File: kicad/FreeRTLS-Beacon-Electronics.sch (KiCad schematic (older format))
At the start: 29 parts, among them J1 USB_B_Micro, J2 TC2030, U1 STM32F072CBTx, U2 NCP1117-3.3_SOT223, U3 DWM1001

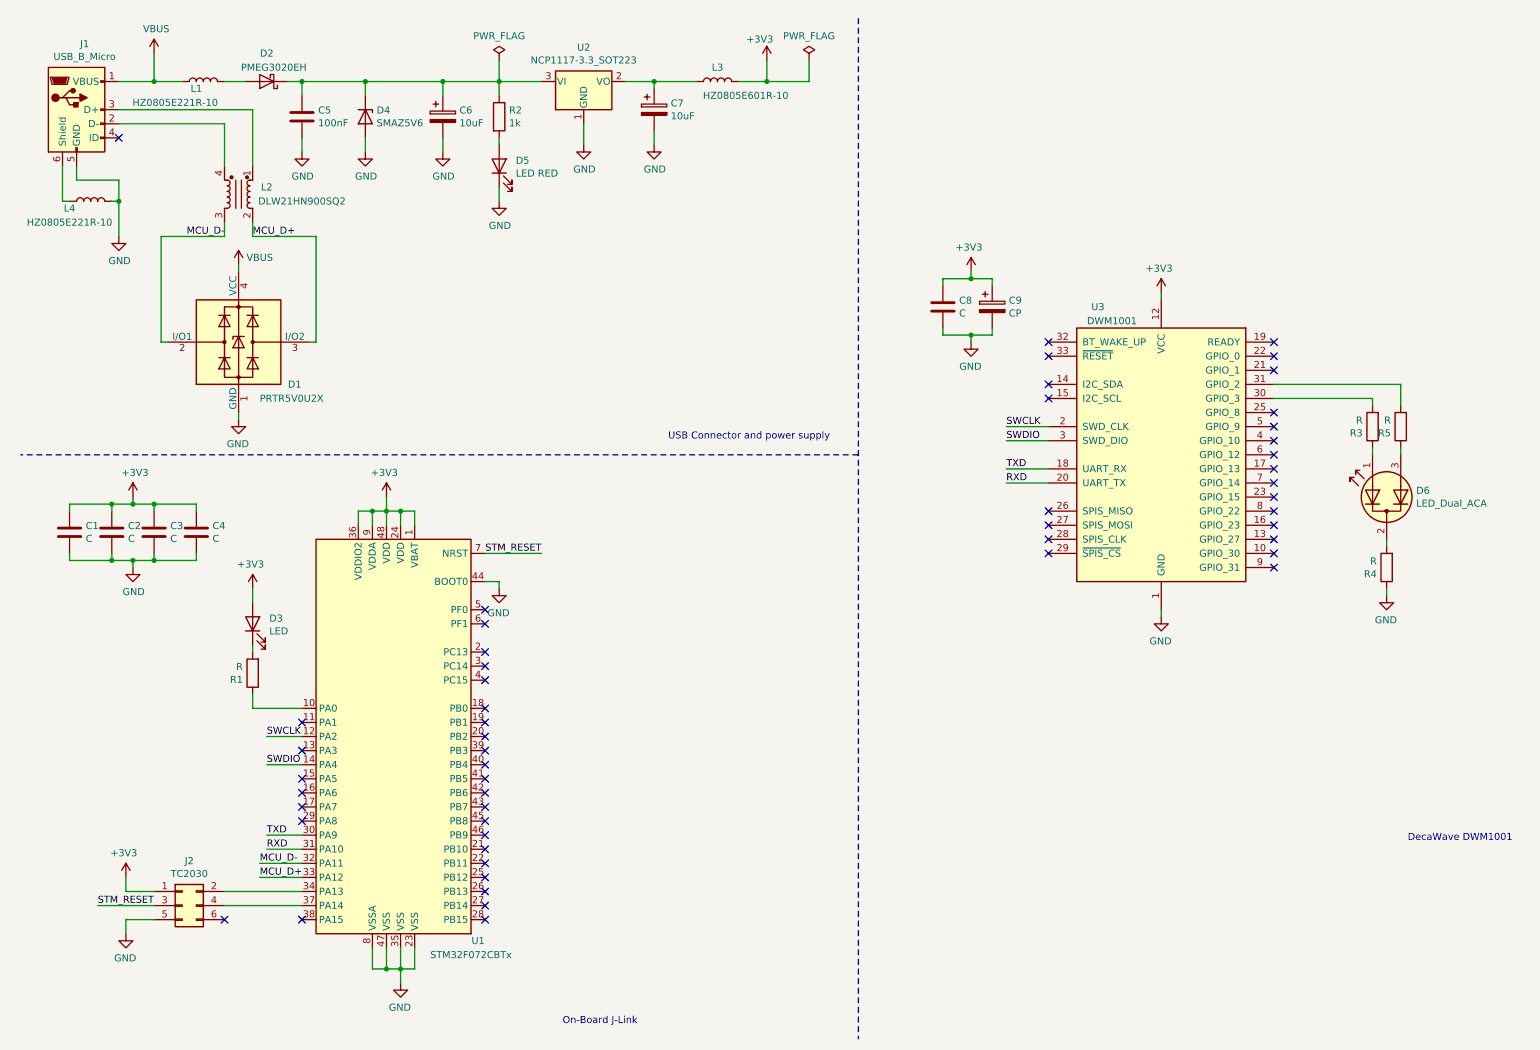
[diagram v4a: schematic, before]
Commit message: Add values and order labels
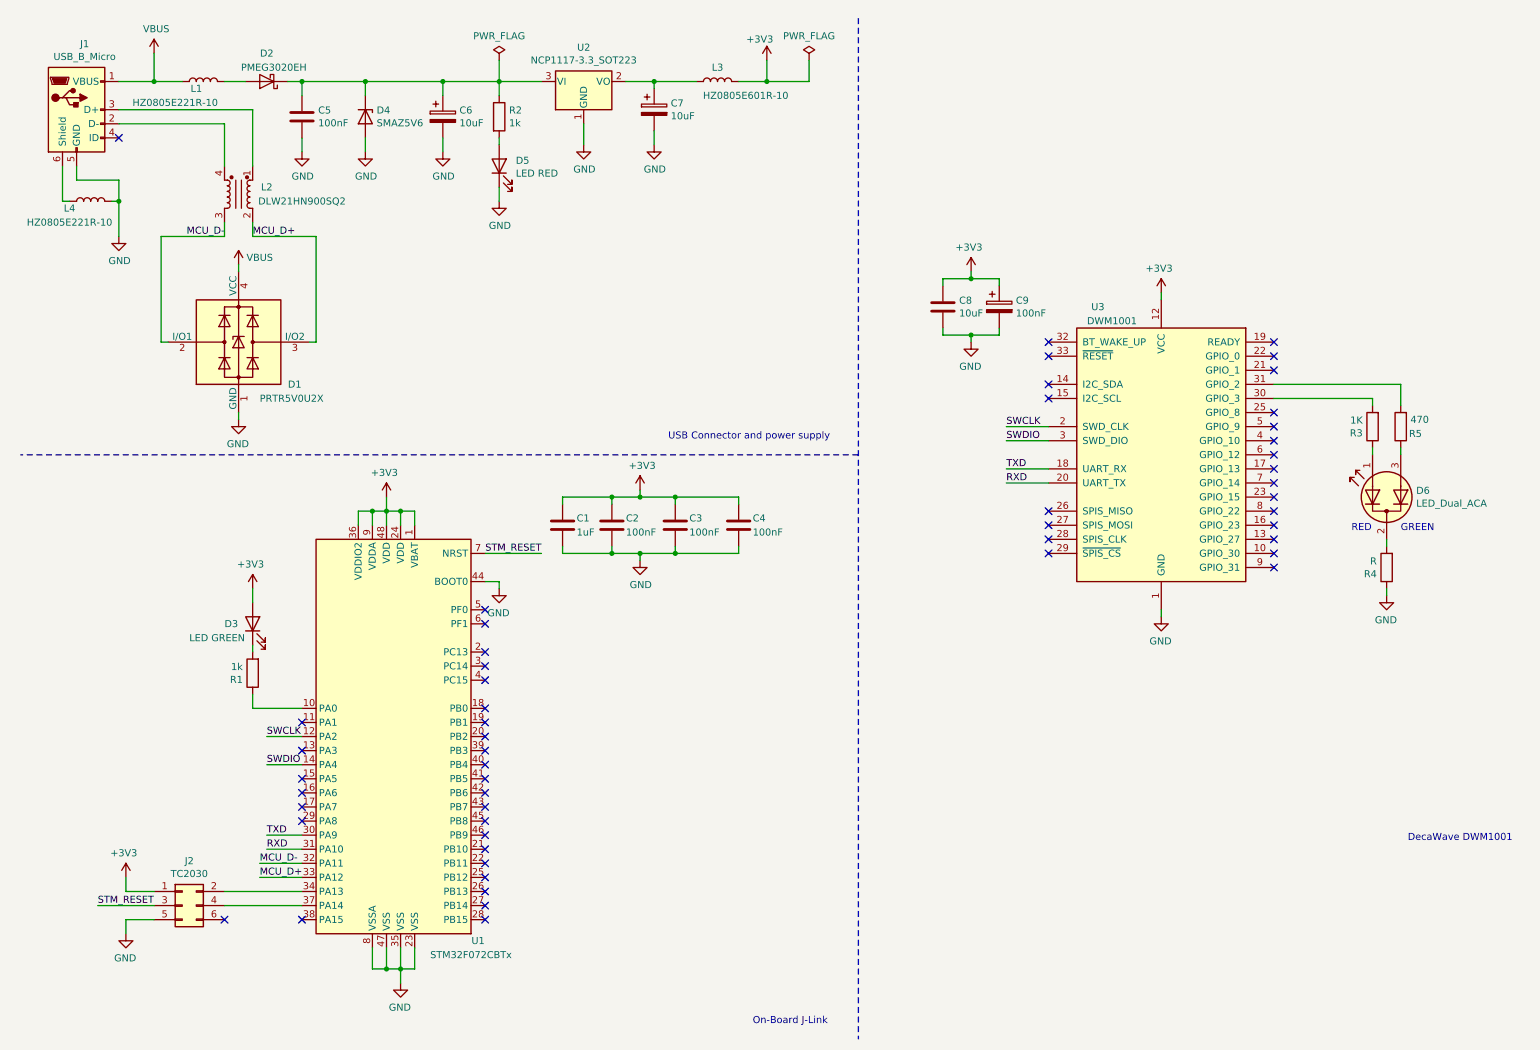
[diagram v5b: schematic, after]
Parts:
- C1: value C -> 1uF
- C2, C3, C4: value C -> 100nF
- C8: value C -> 10uF
- C9: value CP -> 100nF
- D3: value LED -> LED GREEN
- R1: value R -> 1k
- R3: value R -> 1K
- R5: value R -> 470
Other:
- note added: "GREEN"
- note added: "RED"
- moved on the sheet: C1, C2, C3, C4, C9
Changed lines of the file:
@@
 L Device:C C1
 U 1 1 5F5197C4
-P 850 4200
-F 0 "C1" H 965 4246 50  0000 L CNN
-F 1 "C" H 965 4155 50  0000 L CNN
-F 2 "" H 888 4050 50  0001 C CNN
-F 3 "~" H 850 4200 50  0001 C CNN
-	1    850  4200
+P 4350 4150
+F 0 "C1" H 4450 4200 50  0000 L CNN
+F 1 "1uF" H 4450 4100 50  0000 L CNN
+F 2 "" H 4388 4000 50  0001 C CNN
+F 3 "~" H 4350 4150 50  0001 C CNN
+	1    4350 4150
 	1    0    0    -1
 $EndComp
@@
 L Device:C C2
 U 1 1 5F51A6EE
-P 1150 4200
-F 0 "C2" H 1265 4246 50  0000 L CNN
-F 1 "C" H 1265 4155 50  0000 L CNN
-F 2 "" H 1188 4050 50  0001 C CNN
-F 3 "~" H 1150 4200 50  0001 C CNN
-	1    1150 4200
+P 4700 4150
+F 0 "C2" H 4800 4200 50  0000 L CNN
+F 1 "100nF" H 4800 4100 50  0000 L CNN
+F 2 "" H 4738 4000 50  0001 C CNN
+F 3 "~" H 4700 4150 50  0001 C CNN
+	1    4700 4150
 	1    0    0    -1
 $EndComp
@@
 L Device:C C3
 U 1 1 5F51B88B
-P 1450 4200
-F 0 "C3" H 1565 4246 50  0000 L CNN
-F 1 "C" H 1565 4155 50  0000 L CNN
-F 2 "" H 1488 4050 50  0001 C CNN
-F 3 "~" H 1450 4200 50  0001 C CNN
-	1    1450 4200
+P 5150 4150
+F 0 "C3" H 5250 4200 50  0000 L CNN
+F 1 "100nF" H 5250 4100 50  0000 L CNN
+F 2 "" H 5188 4000 50  0001 C CNN
+F 3 "~" H 5150 4150 50  0001 C CNN
+	1    5150 4150
 	1    0    0    -1
 $EndComp
@@
 L Device:C C4
 U 1 1 5F51B891
-P 1750 4200
-F 0 "C4" H 1865 4246 50  0000 L CNN
-F 1 "C" H 1865 4155 50  0000 L CNN
-F 2 "" H 1788 4050 50  0001 C CNN
-F 3 "~" H 1750 4200 50  0001 C CNN
-	1    1750 4200
-	1    0    0    -1
-$EndComp
-Wire Wire Line
-	850  4000 850  4050
-Wire Wire Line
-	850  4000 1150 4000
-Wire Wire Line
-	1750 4000 1750 4050
-Wire Wire Line
-	1450 4050 1450 4000
-Connection ~ 1450 4000
-Wire Wire Line
-	1450 4000 1750 4000
-Wire Wire Line
-	1150 4050 1150 4000
-Connection ~ 1150 4000
-Wire Wire Line
-	1150 4000 1300 4000
-Wire Wire Line
-	850  4350 850  4400
-Wire Wire Line
-	850  4400 1150 4400
-Wire Wire Line
-	1750 4400 1750 4350
-Wire Wire Line
-	1150 4350 1150 4400
-Wire Wire Line
-	1150 4400 1300 4400
-Wire Wire Line
-	1450 4350 1450 4400
-Connection ~ 1450 4400
-Wire Wire Line
-	1450 4400 1750 4400
+P 5600 4150
+F 0 "C4" H 5700 4200 50  0000 L CNN
+F 1 "100nF" H 5700 4100 50  0000 L CNN
+F 2 "" H 5638 4000 50  0001 C CNN
+F 3 "~" H 5600 4150 50  0001 C CNN
+	1    5600 4150
+	1    0    0    -1
+$EndComp
+Wire Wire Line
+	4350 3950 4350 4000
+Wire Wire Line
+	4350 3950 4700 3950
+Wire Wire Line
+	5600 3950 5600 4000
+Wire Wire Line
+	5150 4000 5150 3950
+Connection ~ 5150 3950
+Wire Wire Line
+	5150 3950 5600 3950
+Wire Wire Line
+	4700 4000 4700 3950
+Connection ~ 4700 3950
+Wire Wire Line
+	4700 3950 4900 3950
+Wire Wire Line
+	4350 4300 4350 4350
+Wire Wire Line
+	4350 4350 4700 4350
+Wire Wire Line
+	5600 4350 5600 4300
+Wire Wire Line
+	4700 4300 4700 4350
+Wire Wire Line
+	4700 4350 4900 4350
+Wire Wire Line
+	5150 4300 5150 4350
+Connection ~ 5150 4350
+Wire Wire Line
+	5150 4350 5600 4350
 $Comp
 L power:+3V3 #PWR05
 U 1 1 5F520C3E
-P 1300 3950
-F 0 "#PWR05" H 1300 3800 50  0001 C CNN
-F 1 "+3V3" H 1315 4123 50  0000 C CNN
-F 2 "" H 1300 3950 50  0001 C CNN
-F 3 "" H 1300 3950 50  0001 C CNN
-	1    1300 3950
-	1    0    0    -1
-$EndComp
-Wire Wire Line
-	1300 3950 1300 4000
-Connection ~ 1300 4000
-Wire Wire Line
-	1300 4000 1450 4000
+P 4900 3900
+F 0 "#PWR05" H 4900 3750 50  0001 C CNN
+F 1 "+3V3" H 4915 4073 50  0000 C CNN
+F 2 "" H 4900 3900 50  0001 C CNN
+F 3 "" H 4900 3900 50  0001 C CNN
+	1    4900 3900
+	1    0    0    -1
+$EndComp
+Wire Wire Line
+	4900 3900 4900 3950
+Connection ~ 4900 3950
+Wire Wire Line
+	4900 3950 5150 3950
 $Comp
 L power:GND #PWR06
 U 1 1 5F522893
-P 1300 4450
-F 0 "#PWR06" H 1300 4200 50  0001 C CNN
-F 1 "GND" H 1305 4277 50  0000 C CNN
-F 2 "" H 1300 4450 50  0001 C CNN
-F 3 "" H 1300 4450 50  0001 C CNN
-	1    1300 4450
-	1    0    0    -1
-$EndComp
-Wire Wire Line
-	1300 4450 1300 4400
-Connection ~ 1300 4400
-Wire Wire Line
-	1300 4400 1450 4400
+P 4900 4400
+F 0 "#PWR06" H 4900 4150 50  0001 C CNN
+F 1 "GND" H 4905 4227 50  0000 C CNN
+F 2 "" H 4900 4400 50  0001 C CNN
+F 3 "" H 4900 4400 50  0001 C CNN
+	1    4900 4400
+	1    0    0    -1
+$EndComp
+Wire Wire Line
+	4900 4400 4900 4350
+Connection ~ 4900 4350
+Wire Wire Line
+	4900 4350 5150 4350
 $Comp
 L MCU_ST_STM32F0:STM32F072CBTx U1
@@
 	-1   0    0    -1
 $EndComp
-Connection ~ 1150 4400
+Connection ~ 4700 4350
 Text Label 2200 6550 0    50   ~ 0
 MCU_D-
@@
 P 2150 5200
 F 0 "R1" H 2220 5246 50  0000 L CNN
-F 1 "R" H 2220 5155 50  0000 L CNN
+F 1 "1k" H 2220 5155 50  0000 L CNN
 F 2 "" V 2080 5200 50  0001 C CNN
 F 3 "~" H 2150 5200 50  0001 C CNN
@@
 U 1 1 5F5684FF
 P 2150 4850
-F 0 "D3" V 2189 4732 50  0000 R CNN
-F 1 "LED" V 2098 4732 50  0000 R CNN
+F 0 "D3" V 2150 5050 50  0000 R CNN
+F 1 "LED GREEN" V 2050 5300 50  0000 R CNN
 F 2 "" H 2150 4850 50  0001 C CNN
 F 3 "~" H 2150 4850 50  0001 C CNN
@@
 Wire Wire Line
 	3100 4050 3200 4050
-Text Notes 4350 7700 0    50   ~ 0
+Text Notes 5700 7700 0    50   ~ 0
 On-Board J-Link
 $Comp
@@
 P 10100 3450
 F 0 "R3" H 10170 3496 50  0000 L CNN
-F 1 "R" H 10170 3405 50  0000 L CNN
+F 1 "1K" H 10170 3405 50  0000 L CNN
 F 2 "" V 10030 3450 50  0001 C CNN
 F 3 "~" H 10100 3450 50  0001 C CNN
@@
 U 1 1 5F783AC0
 P 10300 3450
-F 0 "R5" H 10370 3496 50  0000 L CNN
-F 1 "R" H 10370 3405 50  0000 L CNN
+F 0 "R5" H 10150 3500 50  0000 L CNN
+F 1 "470" H 10100 3400 50  0000 L CNN
 F 2 "" V 10230 3450 50  0001 C CNN
 F 3 "~" H 10300 3450 50  0001 C CNN
@@
 L Device:CP C9
 U 1 1 5F7B58BA
-P 7400 2600
-F 0 "C9" H 7518 2646 50  0000 L CNN
-F 1 "CP" H 7518 2555 50  0000 L CNN
-F 2 "" H 7438 2450 50  0001 C CNN
-F 3 "~" H 7400 2600 50  0001 C CNN
-	1    7400 2600
+P 7450 2600
+F 0 "C9" H 7568 2646 50  0000 L CNN
+F 1 "100nF" H 7568 2555 50  0000 L CNN
+F 2 "" H 7488 2450 50  0001 C CNN
+F 3 "~" H 7450 2600 50  0001 C CNN
+	1    7450 2600
 	1    0    0    -1
 $EndComp
@@
 P 7050 2600
 F 0 "C8" H 7165 2646 50  0000 L CNN
-F 1 "C" H 7165 2555 50  0000 L CNN
+F 1 "10uF" H 7165 2555 50  0000 L CNN
 F 2 "" H 7088 2450 50  0001 C CNN
 F 3 "~" H 7050 2600 50  0001 C CNN
@@
 	7050 2400 7250 2400
 Wire Wire Line
-	7400 2400 7400 2450
+	7450 2400 7450 2450
 Wire Wire Line
 	7250 2350 7250 2400
 Connection ~ 7250 2400
 Wire Wire Line
-	7250 2400 7400 2400
+	7250 2400 7450 2400
 Wire Wire Line
 	7050 2800 7250 2800
 Wire Wire Line
-	7400 2800 7400 2750
+	7450 2800 7450 2750
 Wire Wire Line
 	7050 2750 7050 2800
@@
 Connection ~ 7250 2800
 Wire Wire Line
-	7250 2800 7400 2800
+	7250 2800 7450 2800
 Text Notes 10350 6400 0    50   ~ 0
 DecaWave DWM1001
@@
 Wire Wire Line
 	1950 1300 1950 1600
+Text Notes 9950 4200 0    50   ~ 0
+RED
+Text Notes 10300 4200 0    50   ~ 0
+GREEN
 $EndSCHEMATC

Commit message: Fill manufacturer data
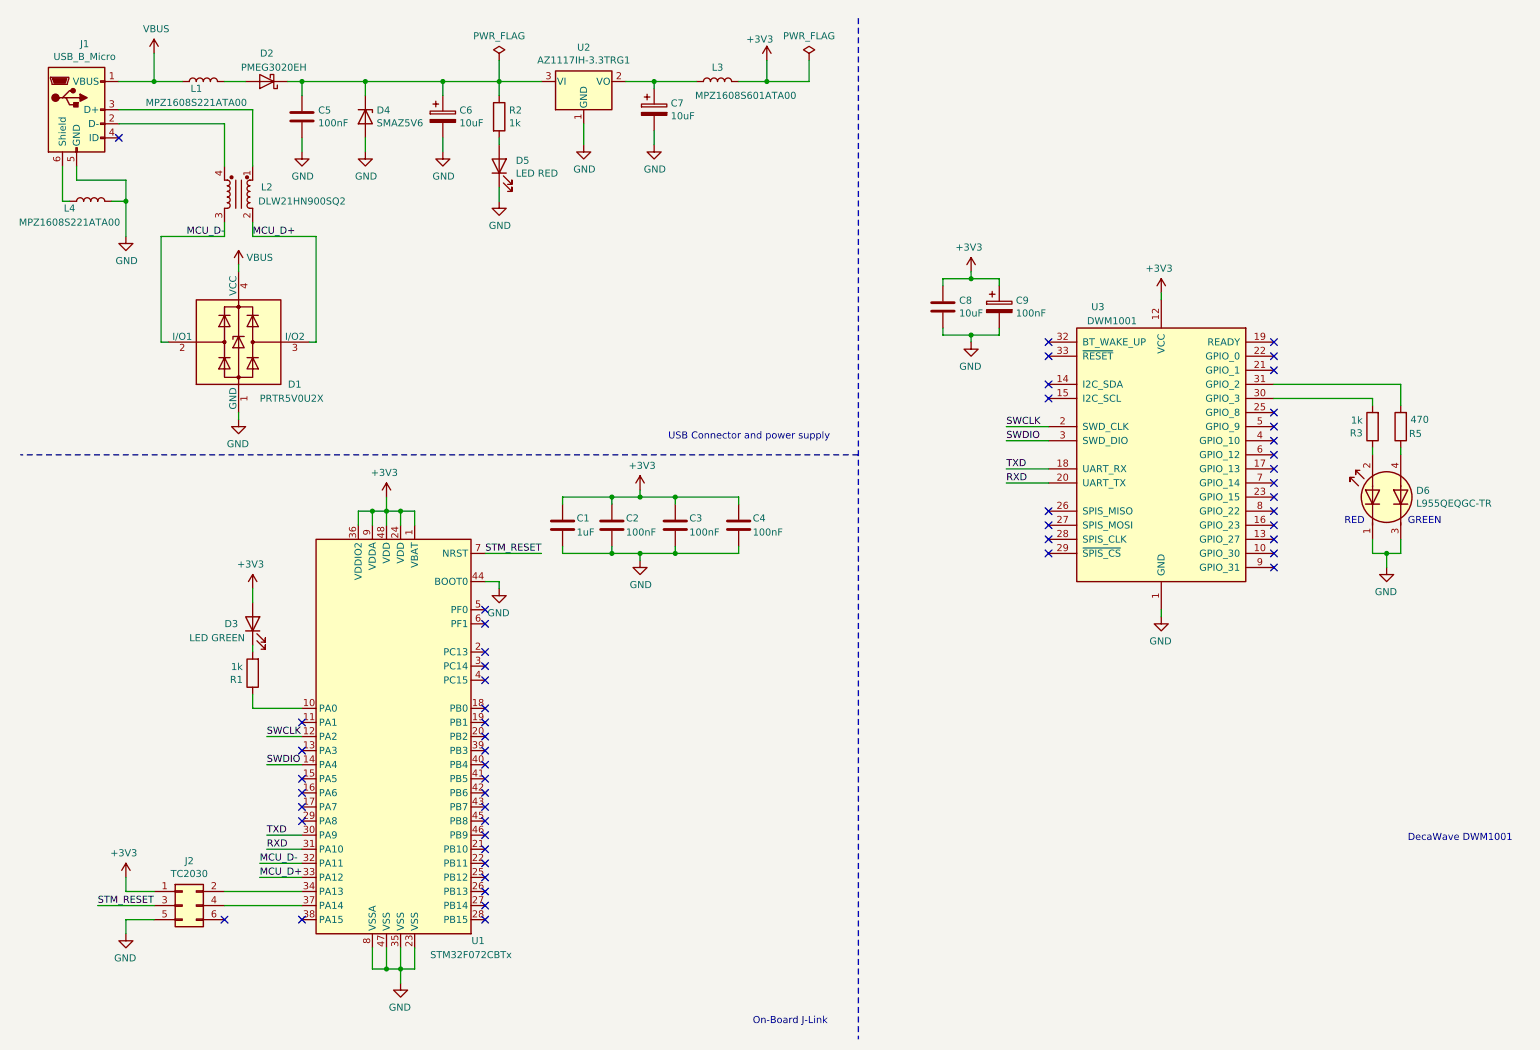
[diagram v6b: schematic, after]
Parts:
- removed D6: LED_Dual_ACA, symbol Device:LED_Dual_ACA
- removed R4: R, symbol Device:R
- added D6: L955QEQGC-TR, symbol Device:LED_Dual_CACA
- C1: DK_Detail_Page (none) -> https://www.digikey.com/en/products/detail/samsung-electro-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; Digi-Key_PN (none) -> 1276-1182-1-ND; MPN (none) -> CL10A105KP8NNNC; Manufacturer (none) -> Samsung Electro-Mechanics
- C2, C3, C4, C5, C9: DK_Detail_Page (none) -> https://www.digikey.com/en/products/detail/kemet/C0603C104Z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; Digi-Key_PN (none) -> 399-1100-1-ND; MPN (none) -> C0603C104Z3VACTU; Manufacturer (none) -> KEMET
- C6, C7, C8: DK_Detail_Page (none) -> https://www.digikey.com/en/products/detail/venkel/C0603X6S1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; Digi-Key_PN (none) -> 2679-C0603X6S100-106MNPTR-ND; MPN (none) -> C0603X6S100-106MNP; Manufacturer (none) -> Venkel
- D1: DK_Detail_Page (none) -> https://www.digikey.com/en/products/detail/nexperia-usa-inc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; Digi-Key_PN (none) -> 1727-3884-1-ND; MPN (none) -> PRTR5V0U2X,215; Manufacturer (none) -> Nexperia USA Inc.
- D2: DK_Detail_Page (none) -> https://www.digikey.com/en/products/detail/nexperia-usa-inc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; Digi-Key_PN (none) -> 1727-3873-1-ND; MPN (none) -> PMEG3020EH,115; Manufacturer (none) -> Nexperia USA Inc.
- D3: DK_Detail_Page (none) -> https://www.digikey.com/en/products/detail/w%C3%BCrth-elekt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; Digi-Key_PN (none) -> 732-4971-1-ND; MPN (none) -> 150060GS75000; Manufacturer (none) -> Würth Elektronik
- D4: DK_Detail_Page (none) -> https://www.digikey.com/en/products/detail/micro-commercial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; Digi-Key_PN (none) -> SMAZ5V6-TPMSCT-ND; MPN (none) -> SMAZ5V6-TP; Manufacturer (none) -> Micro Commercial Co
- D5: DK_Detail_Page (none) -> https://www.digikey.com/en/products/detail/w%C3%BCrth-elekt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; Digi-Key_PN (none) -> 732-4978-1-ND; MPN (none) -> 150060RS75000; Manufacturer (none) -> Würth Elektronik
- J1: footprint (none) -> Connector_USB:USB_Micro-B_Molex_47346-0001; DK_Detail_Page (none) -> https://www.digikey.com/en/products/detail/molex/0473460001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; Digi-Key_PN (none) -> WM17141CT-ND; MPN (none) -> 0473460001; Manufacturer (none) -> Molex
- L1, L4: value HZ0805E221R-10 -> MPZ1608S221ATA00; DK_Detail_Page (none) -> https://www.digikey.com/en/products/detail/tdk-corporation/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; Digi-Key_PN (none) -> 445-1565-1-ND; MPN (none) -> MPZ1608S221ATA00; Manufacturer (none) -> TDK Corporation
- L2: DK_Detail_Page (none) -> https://www.digikey.com/en/products/detail/murata-electroni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; Digi-Key_PN (none) -> 490-1064-1-ND; MPN (none) -> DLW21HN900SQ2L; Manufacturer (none) -> Murata Electronics
- L3: value HZ0805E601R-10 -> MPZ1608S601ATA00; DK_Detail_Page (none) -> https://www.digikey.com/en/products/detail/tdk-corporation/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; Digi-Key_PN (none) -> 445-2205-1-ND; MPN (none) -> MPZ1608S601ATA00; Manufacturer (none) -> TDK Corporation
- R1, R2: DK_Detail_Page (none) -> https://www.digikey.com/en/products/detail/yageo/RC0603JR-0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; Digi-Key_PN (none) -> 311-1.0KGRCT-ND; MPN (none) -> RC0603JR-071KL; Manufacturer (none) -> Yageo
- R3: value 1K -> 1k; DK_Detail_Page (none) -> https://www.digikey.com/en/products/detail/yageo/RC0603JR-0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; Digi-Key_PN (none) -> 311-1.0KGRCT-ND; MPN (none) -> RC0603JR-071KL; Manufacturer (none) -> Yageo
- R5: DK_Detail_Page (none) -> https://www.digikey.com/en/products/detail/yageo/RC0603JR-0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; Digi-Key_PN (none) -> 311-470GRCT-ND; MPN (none) -> RC0603JR-07470RL; Manufacturer (none) -> Yageo
- U1: DK_Detail_Page (none) -> https://www.digikey.com/en/products/detail/stmicroelectroni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; Digi-Key_PN (none) -> 497-17358-ND; MPN (none) -> STM32F072C8T6; Manufacturer (none) -> STMicroelectronics
- U2: value NCP1117-3.3_SOT223 -> AZ1117IH-3.3TRG1; DK_Detail_Page (none) -> https://www.digikey.com/en/products/detail/diodes-incorpora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; Digi-Key_PN (none) -> AZ1117IH-3.3TRG1DICT-ND; MPN (none) -> AZ1117IH-3.3TRG1; Manufacturer (none) -> Diodes Incorporated
- U3: DK_Detail_Page (none) -> https://www.digikey.com/en/products/detail/decawave-limited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; Digi-Key_PN (none) -> 1479-1004-1-ND; MPN (none) -> DWM1001C; Manufacturer (none) -> Decawave Limited
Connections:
- net GND: now also D6.1 (A1), D6.3 (A2)
- net at R3.1: now also D6.2 (K1)
- net at R5.1: now also D6.4 (K2)
